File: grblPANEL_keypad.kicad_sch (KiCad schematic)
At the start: 20 parts, among them J601 Conn_02x10_Odd_Even, U601 ADP5589

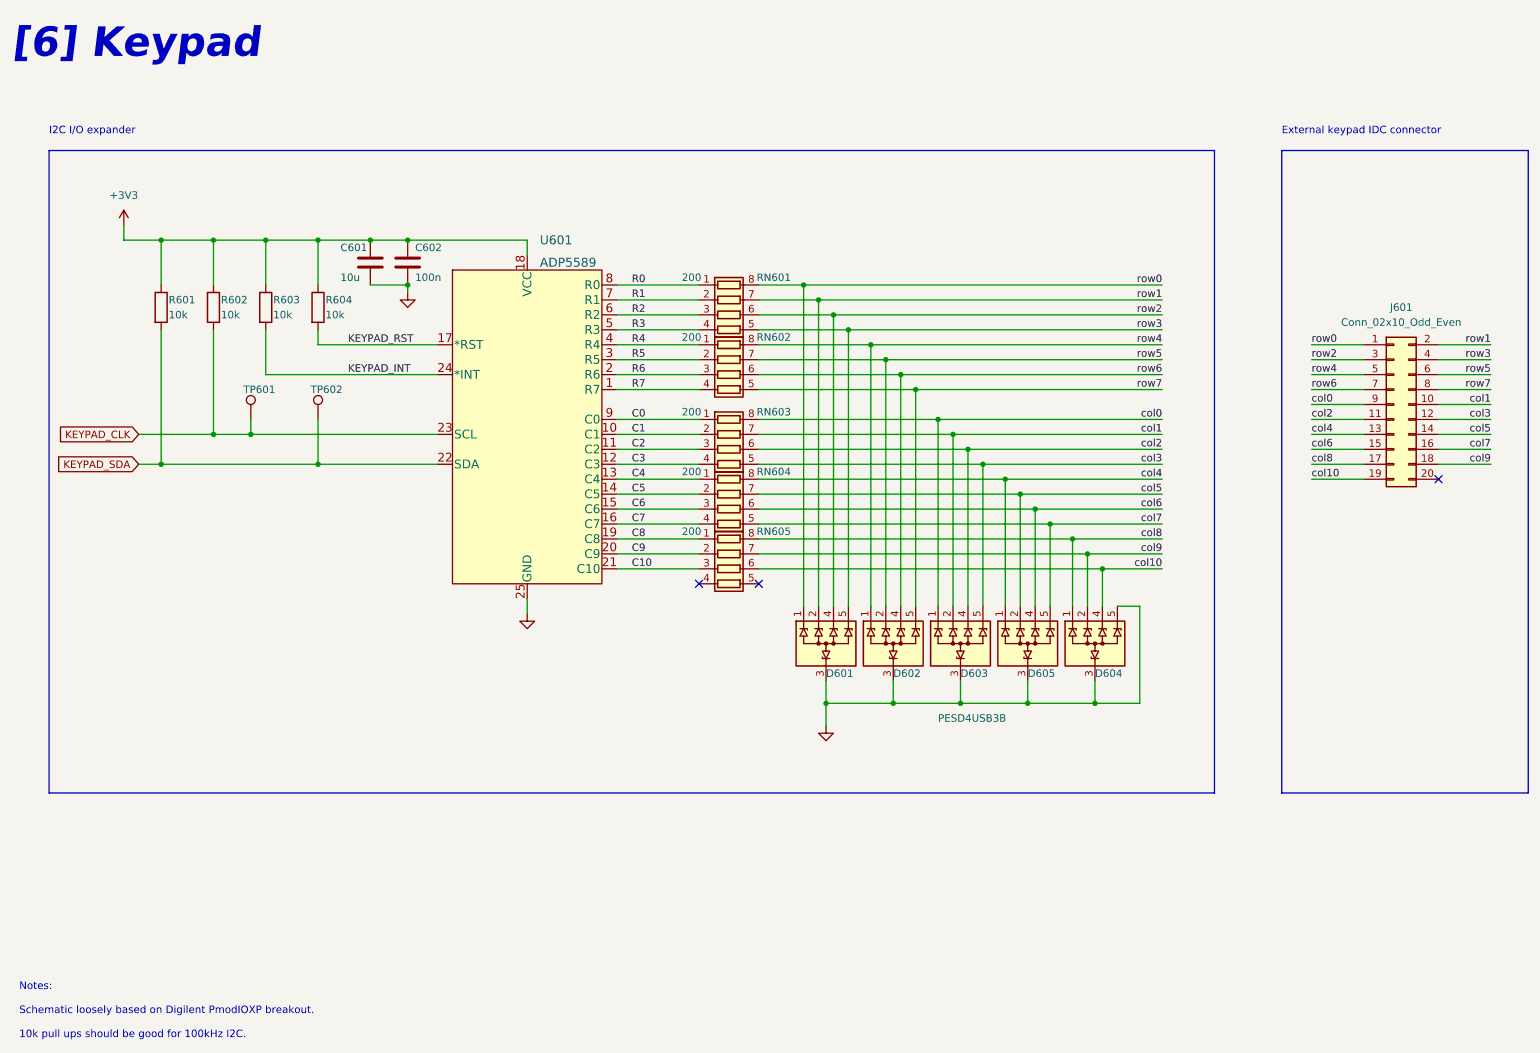
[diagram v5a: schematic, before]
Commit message: 1st stab at routing power input section
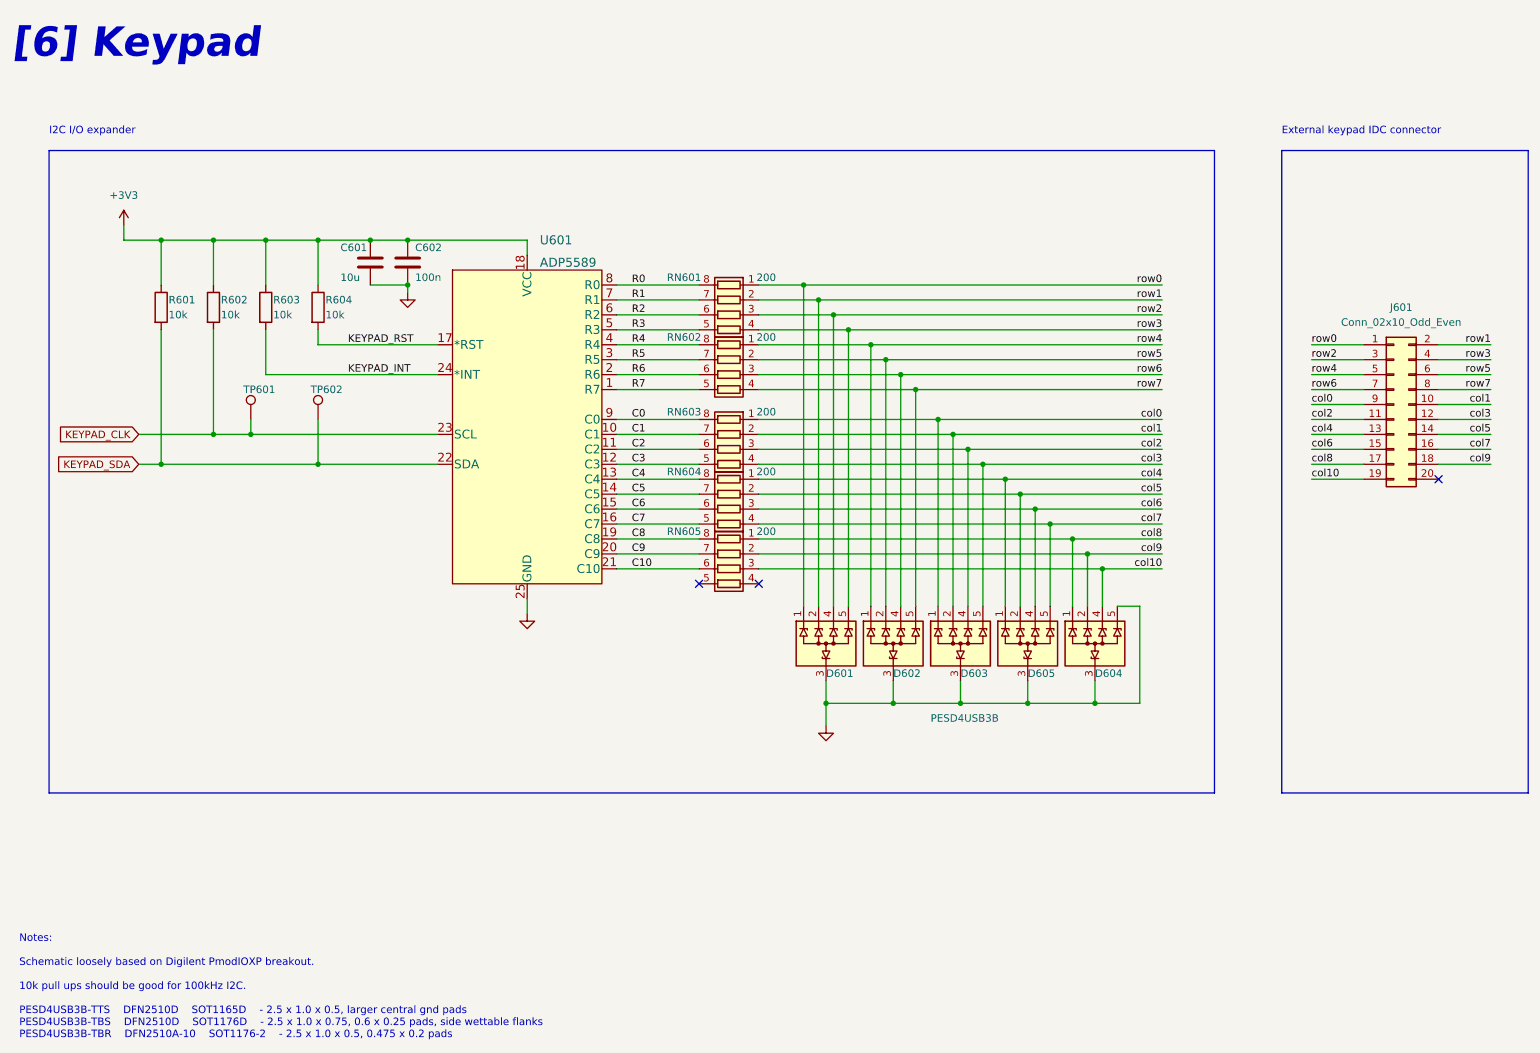
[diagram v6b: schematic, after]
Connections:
- net C0: now also RN603.8 (R1.2); no longer RN603.1 (R1.1)
- net C1: now also RN603.7 (R2.2); no longer RN603.2 (R2.1)
- net C10: now also RN605.6 (R3.2); no longer RN605.3 (R3.1)
- net C2: now also RN603.6 (R3.2); no longer RN603.3 (R3.1)
- net C3: now also RN603.5 (R4.2); no longer RN603.4 (R4.1)
- net C4: now also RN604.8 (R1.2); no longer RN604.1 (R1.1)
- net C5: now also RN604.7 (R2.2); no longer RN604.2 (R2.1)
- net C6: now also RN604.6 (R3.2); no longer RN604.3 (R3.1)
- net C7: now also RN604.5 (R4.2); no longer RN604.4 (R4.1)
- net C8: now also RN605.8 (R1.2); no longer RN605.1 (R1.1)
- net C9: now also RN605.7 (R2.2); no longer RN605.2 (R2.1)
- net R0: now also RN601.8 (R1.2); no longer RN601.1 (R1.1)
- net R1: now also RN601.7 (R2.2); no longer RN601.2 (R2.1)
- net R2: now also RN601.6 (R3.2); no longer RN601.3 (R3.1)
- net R3: now also RN601.5 (R4.2); no longer RN601.4 (R4.1)
- net R4: now also RN602.8 (R1.2); no longer RN602.1 (R1.1)
- net R5: now also RN602.7 (R2.2); no longer RN602.2 (R2.1)
- net R6: now also RN602.6 (R3.2); no longer RN602.3 (R3.1)
- net R7: now also RN602.5 (R4.2); no longer RN602.4 (R4.1)
- net col0: now also RN603.1 (R1.1); no longer RN603.8 (R1.2)
- net col1: now also RN603.2 (R2.1); no longer RN603.7 (R2.2)
- net col10: now also RN605.3 (R3.1); no longer RN605.6 (R3.2)
- net col2: now also RN603.3 (R3.1); no longer RN603.6 (R3.2)
- net col3: now also RN603.4 (R4.1); no longer RN603.5 (R4.2)
- net col4: now also RN604.1 (R1.1); no longer RN604.8 (R1.2)
- net col5: now also RN604.2 (R2.1); no longer RN604.7 (R2.2)
- net col6: now also RN604.3 (R3.1); no longer RN604.6 (R3.2)
- net col7: now also RN604.4 (R4.1); no longer RN604.5 (R4.2)
- net col8: now also RN605.1 (R1.1); no longer RN605.8 (R1.2)
- net col9: now also RN605.2 (R2.1); no longer RN605.7 (R2.2)
- net row0: now also RN601.1 (R1.1); no longer RN601.8 (R1.2)
- net row1: now also RN601.2 (R2.1); no longer RN601.7 (R2.2)
- net row2: now also RN601.3 (R3.1); no longer RN601.6 (R3.2)
- net row3: now also RN601.4 (R4.1); no longer RN601.5 (R4.2)
- net row4: now also RN602.1 (R1.1); no longer RN602.8 (R1.2)
- net row5: now also RN602.2 (R2.1); no longer RN602.7 (R2.2)
- net row6: now also RN602.3 (R3.1); no longer RN602.6 (R3.2)
- net row7: now also RN602.4 (R4.1); no longer RN602.5 (R4.2)
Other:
- note added: "Notes: Schematic loosely based on Digilent PmodIOXP breakout. 10k pull ups should be good for 100kHz I2C. PESD4USB3B-TTS DFN2510D SOT1165D - 2.5 x 1.0 x 0.5, larger central gnd pads PESD4USB3B-TBS DFN2510D SOT1176D - 2.5 x 1.0 x 0.75, 0.6 x 0.25 pads, side wettable flanks PESD4USB3B-TBR DFN2510A-10 SOT1176-2 - 2.5 x 1.0 x 0.5, 0.475 x 0.2 pads"
- note removed: "Notes: Schematic loosely based on Digilent PmodIOXP breakout. 10k pull ups should be good for 100kHz I2C."
- moved on the sheet: RN601, RN602, RN603, RN604, RN605
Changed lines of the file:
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@@
     (effects (font (size 1.27 1.27)) (justify left bottom))
   )
-  (text "Notes:\n\nSchematic loosely based on Digilent PmodIOXP breakout.\n\n10k pull ups should be good for 100kHz I2C."
+  (text "Notes:\n\nSchematic loosely based on Digilent PmodIOXP breakout.\n\n10k pull ups should be good for 100kHz I2C.\n\nPESD4USB3B-TTS	DFN2510D	SOT1165D	- 2.5 x 1.0 x 0.5, larger central gnd pads\nPESD4USB3B-TBS	DFN2510D	SOT1176D	- 2.5 x 1.0 x 0.75, 0.6 x 0.25 pads, side wettable flanks\nPESD4USB3B-TBR	DFN2510A-10	SOT1176-2	- 2.5 x 1.0 x 0.5, 0.475 x 0.2 pads\n"
     (at 19.05 193.04 0)
     (effects (font (size 1.27 1.27)) (justify left bottom))
@@
     (pin "9")
   )
-  (symbol (lib_id "Device:R_Pack04") (at 139.7 92.71 270) (unit 1)
-    (in_bom yes) (on_board yes)
-    (property "Reference" "RN603" (id 0) (at 147.32 86.36 90))
-    (property "Value" "200" (id 1) (at 133.35 86.36 90))
+  (symbol (lib_id "Device:R_Pack04") (at 139.7 92.71 90) (mirror x) (unit 1)
+    (in_bom yes) (on_board yes)
+    (property "Reference" "RN603" (id 0) (at 132.08 86.36 90))
+    (property "Value" "200" (id 1) (at 146.05 86.36 90))
     (property "Footprint" "Resistor_SMD:R_Array_Concave_4x0603" (id 2) (at 139.7 99.695 90)
       (effects (font (size 1.27 1.27)) hide)
@@
     (pin "1")
   )
-  (symbol (lib_id "Device:R_Pack04") (at 139.7 102.87 270) (unit 1)
-    (in_bom yes) (on_board yes)
-    (property "Reference" "RN604" (id 0) (at 147.32 96.52 90))
-    (property "Value" "200" (id 1) (at 133.35 96.52 90))
+  (symbol (lib_id "Device:R_Pack04") (at 139.7 102.87 90) (mirror x) (unit 1)
+    (in_bom yes) (on_board yes)
+    (property "Reference" "RN604" (id 0) (at 132.08 96.52 90))
+    (property "Value" "200" (id 1) (at 146.05 96.52 90))
     (property "Footprint" "Resistor_SMD:R_Array_Concave_4x0603" (id 2) (at 139.7 109.855 90)
       (effects (font (size 1.27 1.27)) hide)
@@
       (effects (font (size 1.27 1.27)) (justify left))
     )
-    (property "Value" "PESD4USB3B" (id 1) (at 175.26 138.43 0)
+    (property "Value" "PESD4USB3B" (id 1) (at 173.99 138.43 0)
       (effects (font (size 1.27 1.27)) (justify left))
     )
@@
     (pin "1")
   )
-  (symbol (lib_id "Device:R_Pack04") (at 139.7 113.03 270) (unit 1)
-    (in_bom yes) (on_board yes)
-    (property "Reference" "RN605" (id 0) (at 147.32 106.68 90))
-    (property "Value" "200" (id 1) (at 133.35 106.68 90))
+  (symbol (lib_id "Device:R_Pack04") (at 139.7 113.03 90) (mirror x) (unit 1)
+    (in_bom yes) (on_board yes)
+    (property "Reference" "RN605" (id 0) (at 132.08 106.68 90))
+    (property "Value" "200" (id 1) (at 146.05 106.68 90))
     (property "Footprint" "Resistor_SMD:R_Array_Concave_4x0603" (id 2) (at 139.7 120.015 90)
       (effects (font (size 1.27 1.27)) hide)
@@
     (pin "8")
   )
-  (symbol (lib_id "Device:R_Pack04") (at 139.7 69.85 270) (unit 1)
-    (in_bom yes) (on_board yes)
-    (property "Reference" "RN601" (id 0) (at 147.32 63.5 90))
-    (property "Value" "200" (id 1) (at 133.35 63.5 90))
+  (symbol (lib_id "Device:R_Pack04") (at 139.7 69.85 90) (mirror x) (unit 1)
+    (in_bom yes) (on_board yes)
+    (property "Reference" "RN601" (id 0) (at 132.08 63.5 90))
+    (property "Value" "200" (id 1) (at 146.05 63.5 90))
     (property "Footprint" "Resistor_SMD:R_Array_Concave_4x0603" (id 2) (at 139.7 76.835 90)
       (effects (font (size 1.27 1.27)) hide)
@@
     (pin "1")
   )
-  (symbol (lib_id "Device:R_Pack04") (at 139.7 80.01 270) (unit 1)
-    (in_bom yes) (on_board yes)
-    (property "Reference" "RN602" (id 0) (at 147.32 73.66 90))
-    (property "Value" "200" (id 1) (at 133.35 73.66 90))
+  (symbol (lib_id "Device:R_Pack04") (at 139.7 80.01 90) (mirror x) (unit 1)
+    (in_bom yes) (on_board yes)
+    (property "Reference" "RN602" (id 0) (at 132.08 73.66 90))
+    (property "Value" "200" (id 1) (at 146.05 73.66 90))
     (property "Footprint" "Resistor_SMD:R_Array_Concave_4x0603" (id 2) (at 139.7 86.995 90)
       (effects (font (size 1.27 1.27)) hide)

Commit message: power section cleanup change 1206 caps to 0805
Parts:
- C601: footprint Capacitor_SMD:C_1206_3216Metric -> Capacitor_SMD:C_0805_2012Metric
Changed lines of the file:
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@@
       (effects (font (size 1.27 1.27)) (justify left))
     )
-    (property "Footprint" "Capacitor_SMD:C_1206_3216Metric" (id 2) (at 79.7052 64.77 0)
+    (property "Footprint" "Capacitor_SMD:C_0805_2012Metric" (id 2) (at 79.7052 64.77 0)
       (effects (font (size 1.27 1.27)) hide)
     )

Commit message: small cleanups
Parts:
- RN601, RN602, RN603, RN604, RN605: footprint Resistor_SMD:R_Array_Concave_4x0603 -> Resistor_SMD:R_Array_Convex_4x0603
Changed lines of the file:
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@@
     (property "Reference" "RN603" (id 0) (at 132.08 86.36 90))
     (property "Value" "200" (id 1) (at 146.05 86.36 90))
-    (property "Footprint" "Resistor_SMD:R_Array_Concave_4x0603" (id 2) (at 139.7 99.695 90)
+    (property "Footprint" "Resistor_SMD:R_Array_Convex_4x0603" (id 2) (at 139.7 99.695 90)
       (effects (font (size 1.27 1.27)) hide)
     )
@@
     (property "Reference" "RN604" (id 0) (at 132.08 96.52 90))
     (property "Value" "200" (id 1) (at 146.05 96.52 90))
-    (property "Footprint" "Resistor_SMD:R_Array_Concave_4x0603" (id 2) (at 139.7 109.855 90)
+    (property "Footprint" "Resistor_SMD:R_Array_Convex_4x0603" (id 2) (at 139.7 109.855 90)
       (effects (font (size 1.27 1.27)) hide)
     )
@@
     (property "Reference" "RN605" (id 0) (at 132.08 106.68 90))
     (property "Value" "200" (id 1) (at 146.05 106.68 90))
-    (property "Footprint" "Resistor_SMD:R_Array_Concave_4x0603" (id 2) (at 139.7 120.015 90)
+    (property "Footprint" "Resistor_SMD:R_Array_Convex_4x0603" (id 2) (at 139.7 120.015 90)
       (effects (font (size 1.27 1.27)) hide)
     )
@@
     (property "Reference" "RN601" (id 0) (at 132.08 63.5 90))
     (property "Value" "200" (id 1) (at 146.05 63.5 90))
-    (property "Footprint" "Resistor_SMD:R_Array_Concave_4x0603" (id 2) (at 139.7 76.835 90)
+    (property "Footprint" "Resistor_SMD:R_Array_Convex_4x0603" (id 2) (at 139.7 76.835 90)
       (effects (font (size 1.27 1.27)) hide)
     )
@@
     (property "Reference" "RN602" (id 0) (at 132.08 73.66 90))
     (property "Value" "200" (id 1) (at 146.05 73.66 90))
-    (property "Footprint" "Resistor_SMD:R_Array_Concave_4x0603" (id 2) (at 139.7 86.995 90)
-      (effects (font (size 1.27 1.27)) hide)
-    )
+    (property "Footprint" "Resistor_SMD:R_Array_Convex_4x0603" (id 2) (at 139.7 86.995 90)
+      (effects (font (size 1.27 1.27)) hide)
+    )
